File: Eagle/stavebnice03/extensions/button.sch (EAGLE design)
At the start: 4 parts

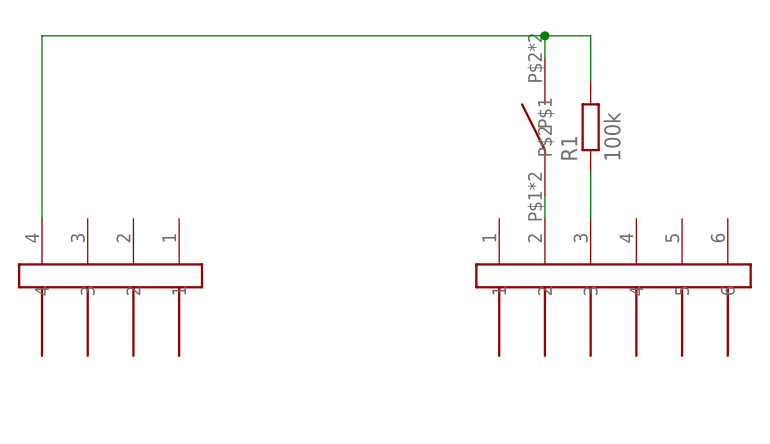
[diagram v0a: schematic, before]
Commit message: eagle adjustment for the Jíťa version
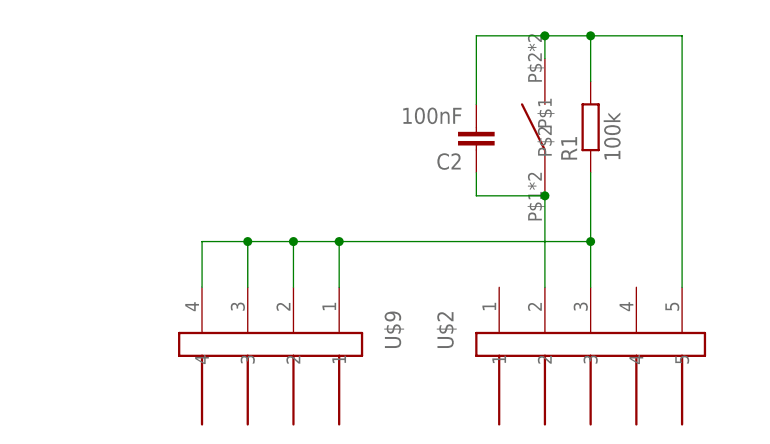
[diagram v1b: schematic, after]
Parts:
- removed U$8: JUMPER6M, !stavebnice03:JUMPER6M
- added C2: 100nF, resistor:C-EUC0603K
- added U$2: JUMPER5M, !stavebnice03:JUMPER5M
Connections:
- removed net N$2: U$1.P$1, U$8.2
- removed net N$3: R1.1, U$8.3
- new net AA: C2.2, R1.2, U$1.P$2, U$2.5
- new net VCC: C2.1, U$1.P$1, U$2.2
- net GND: now also R1.1, U$2.3, U$9.1, U$9.2, U$9.3; no longer R1.2, U$1.P$2
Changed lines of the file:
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@@
 <layer number="98" name="Guide" color="6" fill="1" visible="yes" active="yes"/>
 <layer number="99" name="SpiceOrder" color="5" fill="1" visible="no" active="no"/>
+<layer number="116" name="centerDrill" color="7" fill="1" visible="no" active="yes"/>
 </layers>
 <schematic xreflabel="%F%N/%S.%C%R" xrefpart="/%S.%C%R">
@@
 </classes>
 <parts>
-<part name="U$8" library="!stavebnice03" deviceset="JUMPER6M" device=""/>
 <part name="U$9" library="!stavebnice03" deviceset="JUMPER4M" device=""/>
 <part name="R1" library="resistor" deviceset="R-EU_" device="R0603" value="100k"/>
 <part name="U$1" library="!stavebnice03" deviceset="BUTTON_6.3X6.3" device=""/>
+<part name="U$2" library="!stavebnice03" deviceset="JUMPER5M" device=""/>
+<part name="C2" library="resistor" deviceset="C-EU" device="C0603K" value="100nF"/>
 </parts>
 <sheets>
@@
 </plain>
 <instances>
-<instance part="U$8" gate="G$1" x="175.26" y="35.56" rot="MR270"/>
-<instance part="U$9" gate="G$1" x="119.38" y="35.56" rot="R270"/>
+<instance part="U$9" gate="G$1" x="137.16" y="27.94" rot="R270"/>
 <instance part="R1" gate="G$1" x="172.72" y="53.34" rot="R90"/>
 <instance part="U$1" gate="G$1" x="167.64" y="53.34" rot="R90"/>
+<instance part="U$2" gate="G$1" x="172.72" y="27.94" rot="MR270"/>
+<instance part="C2" gate="G$1" x="160.02" y="50.8" rot="R180"/>
 </instances>
 <busses>
 </busses>
 <nets>
-<net name="GND" class="0">
+<net name="AA" class="0">
 <segment>
 <pinref part="U$1" gate="G$1" pin="P$2"/>
-<wire x1="111.76" y1="63.5" x2="167.64" y2="63.5" width="0.1524" layer="91"/>
+<wire x1="160.02" y1="63.5" x2="167.64" y2="63.5" width="0.1524" layer="91"/>
 <wire x1="167.64" y1="63.5" x2="167.64" y2="60.96" width="0.1524" layer="91"/>
 <wire x1="167.64" y1="63.5" x2="172.72" y2="63.5" width="0.1524" layer="91"/>
@@
 <pinref part="R1" gate="G$1" pin="2"/>
 <wire x1="172.72" y1="58.42" x2="172.72" y2="63.5" width="0.1524" layer="91"/>
-<pinref part="U$9" gate="G$1" pin="4"/>
-<wire x1="111.76" y1="63.5" x2="111.76" y2="43.18" width="0.1524" layer="91"/>
+<pinref part="C2" gate="G$1" pin="2"/>
+<wire x1="160.02" y1="55.88" x2="160.02" y2="63.5" width="0.1524" layer="91"/>
+<pinref part="U$2" gate="G$1" pin="5"/>
+<wire x1="172.72" y1="63.5" x2="182.88" y2="63.5" width="0.1524" layer="91"/>
+<wire x1="182.88" y1="63.5" x2="182.88" y2="35.56" width="0.1524" layer="91"/>
+<junction x="172.72" y="63.5"/>
 </segment>
 </net>
-<net name="N$2" class="0">
+<net name="GND" class="0">
 <segment>
-<pinref part="U$8" gate="G$1" pin="2"/>
-<pinref part="U$1" gate="G$1" pin="P$1"/>
-<wire x1="167.64" y1="43.18" x2="167.64" y2="45.72" width="0.1524" layer="91"/>
+<pinref part="R1" gate="G$1" pin="1"/>
+<wire x1="172.72" y1="48.26" x2="172.72" y2="40.64" width="0.1524" layer="91"/>
+<pinref part="U$2" gate="G$1" pin="3"/>
+<pinref part="U$9" gate="G$1" pin="4"/>
+<wire x1="172.72" y1="40.64" x2="172.72" y2="35.56" width="0.1524" layer="91"/>
+<wire x1="129.54" y1="35.56" x2="129.54" y2="40.64" width="0.1524" layer="91"/>
+<pinref part="U$9" gate="G$1" pin="1"/>
+<wire x1="129.54" y1="40.64" x2="134.62" y2="40.64" width="0.1524" layer="91"/>
+<wire x1="134.62" y1="40.64" x2="139.7" y2="40.64" width="0.1524" layer="91"/>
+<wire x1="139.7" y1="40.64" x2="144.78" y2="40.64" width="0.1524" layer="91"/>
+<wire x1="144.78" y1="40.64" x2="144.78" y2="35.56" width="0.1524" layer="91"/>
+<pinref part="U$9" gate="G$1" pin="2"/>
+<wire x1="139.7" y1="35.56" x2="139.7" y2="40.64" width="0.1524" layer="91"/>
+<pinref part="U$9" gate="G$1" pin="3"/>
+<wire x1="134.62" y1="35.56" x2="134.62" y2="40.64" width="0.1524" layer="91"/>
+<wire x1="144.78" y1="40.64" x2="172.72" y2="40.64" width="0.1524" layer="91"/>
+<junction x="172.72" y="40.64"/>
+<junction x="134.62" y="40.64"/>
+<junction x="139.7" y="40.64"/>
+<junction x="144.78" y="40.64"/>
 </segment>
 </net>
-<net name="N$3" class="0">
+<net name="VCC" class="0">
 <segment>
-<pinref part="R1" gate="G$1" pin="1"/>
-<pinref part="U$8" gate="G$1" pin="3"/>
-<wire x1="172.72" y1="48.26" x2="172.72" y2="43.18" width="0.1524" layer="91"/>
+<pinref part="C2" gate="G$1" pin="1"/>
+<wire x1="160.02" y1="48.26" x2="160.02" y2="45.72" width="0.1524" layer="91"/>
+<pinref part="U$1" gate="G$1" pin="P$1"/>
+<wire x1="167.64" y1="35.56" x2="167.64" y2="45.72" width="0.1524" layer="91"/>
+<pinref part="U$2" gate="G$1" pin="2"/>
+<wire x1="160.02" y1="45.72" x2="167.64" y2="45.72" width="0.1524" layer="91"/>
+<junction x="167.64" y="45.72"/>
 </segment>
 </net>
